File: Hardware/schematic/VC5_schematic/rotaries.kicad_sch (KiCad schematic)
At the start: 9 parts, among them SW1 RotaryEncoder_Switch, SW2 RotaryEncoder_Switch, SW3 RotaryEncoder_Switch, SW4 RotaryEncoder_Switch, SW5 RotaryEncoder_Switch, U7 MCP23017_ML

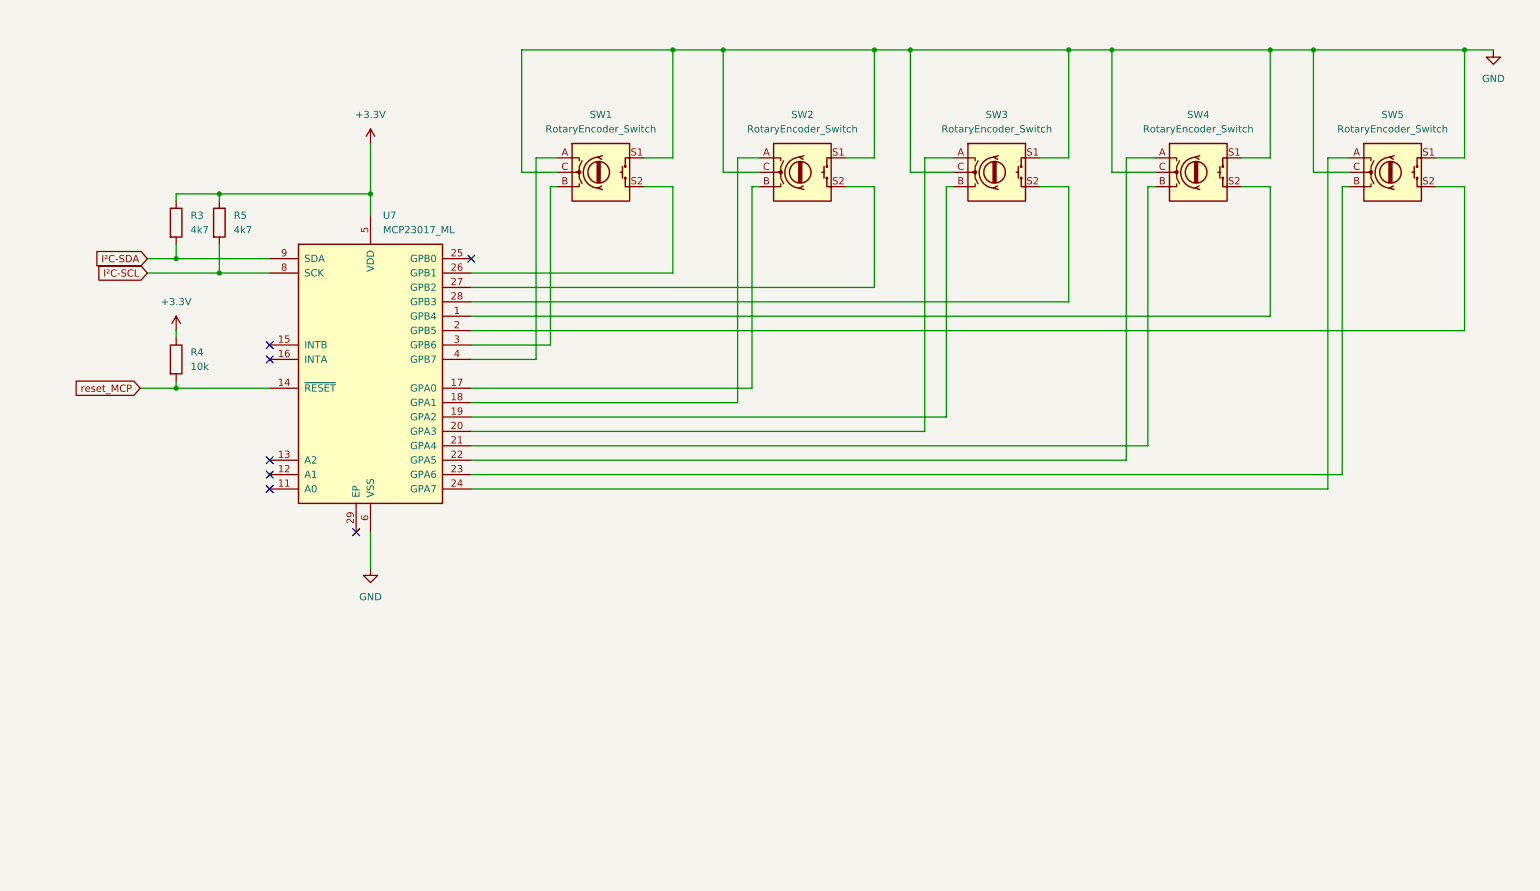
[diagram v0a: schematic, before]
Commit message: minor updates to the schematic
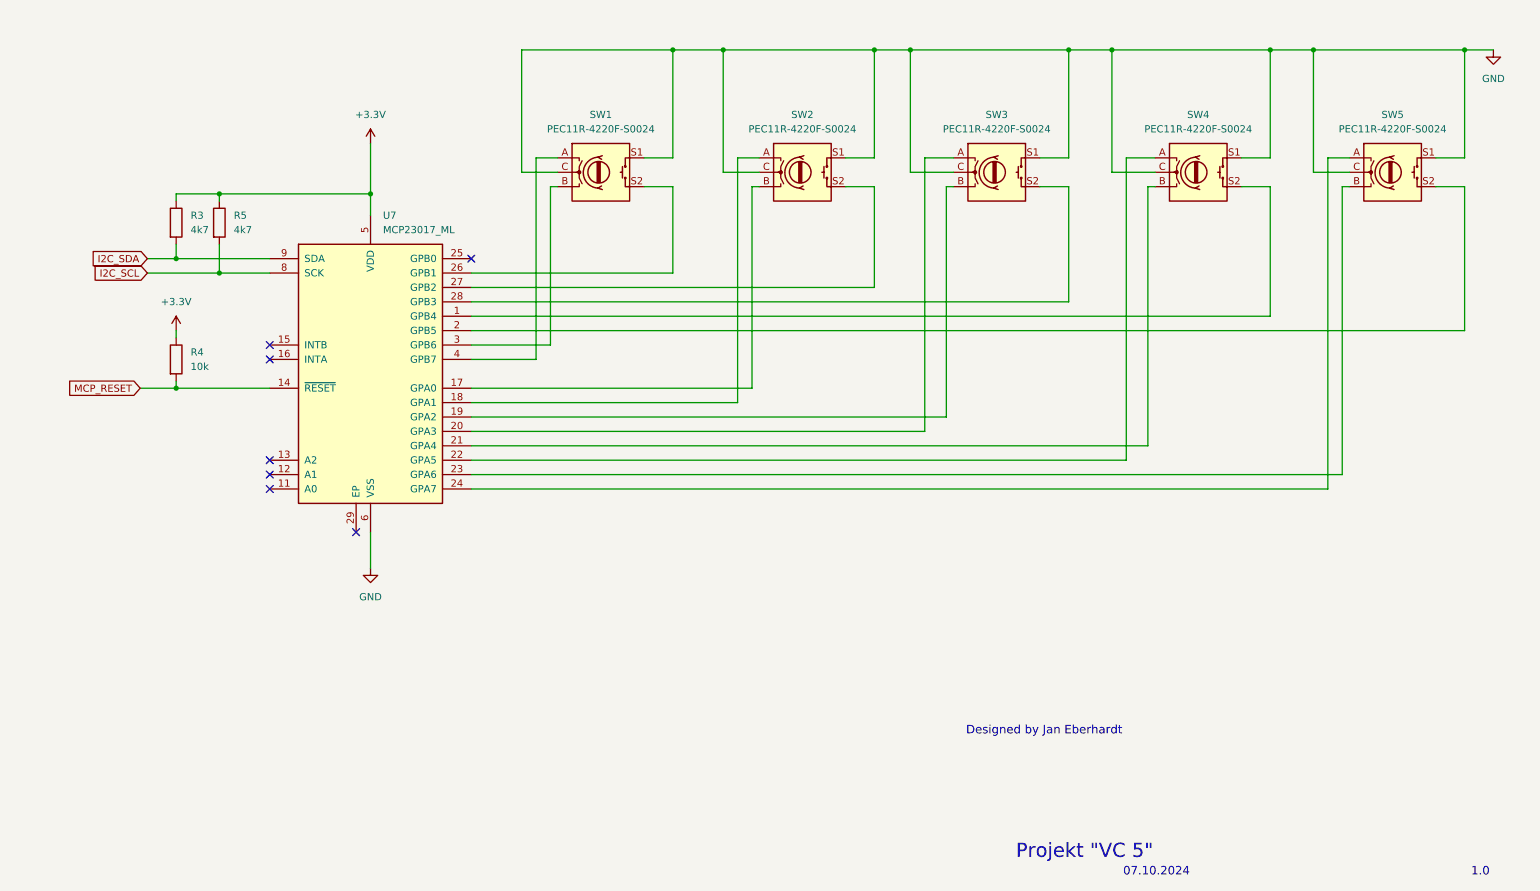
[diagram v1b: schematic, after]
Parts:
- SW1, SW2, SW3, SW4, SW5: value RotaryEncoder_Switch -> PEC11R-4220F-S0024
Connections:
- net I²C-SCL renamed I2C_SCL
- net I²C-SDA renamed I2C_SDA
- net reset_MCP renamed MCP_RESET
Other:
- note added: "07.10.2024"
- note added: "1.0"
- note added: "Designed by Jan Eberhardt"
- note added: "Projekt "VC 5""
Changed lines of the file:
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@@
 		)
 	)
-	(global_label "reset_MCP"
+	(text "Designed by Jan Eberhardt"
+		(exclude_from_sim no)
+		(at 193.802 168.402 0)
+		(effects
+			(font
+				(size 1.5 1.5)
+			)
+		)
+	)
+	(text "07.10.2024"
+		(exclude_from_sim no)
+		(at 213.614 193.294 0)
+		(effects
+			(font
+				(size 1.5 1.5)
+			)
+		)
+	)
+	(text "1.0"
+		(exclude_from_sim no)
+		(at 270.764 193.294 0)
+		(effects
+			(font
+				(size 1.5 1.5)
+			)
+		)
+	)
+	(text "Projekt \"VC 5\""
+		(exclude_from_sim no)
+		(at 200.914 189.738 0)
+		(effects
+			(font
+				(size 2.5 2.5)
+			)
+		)
+	)
+	(global_label "MCP_RESET"
 		(shape input)
 		(at 34.29 107.95 180)
@@
 		)
 		(property "Intersheetrefs" "${INTERSHEET_REFS}"
-			(at 21.6286 107.95 0)
+			(at 21.2549 107.95 0)
 			(effects
 				(font
@@
 		)
 	)
-	(global_label "I²C-SCL"
+	(global_label "I2C_SCL"
 		(shape input)
 		(at 35.56 87.63 180)
@@
 		)
 		(property "Intersheetrefs" "${INTERSHEET_REFS}"
-			(at 24.6524 87.63 0)
+			(at 25.6695 87.63 0)
 			(effects
 				(font
@@
 		)
 	)
-	(global_label "I²C-SDA"
+	(global_label "I2C_SDA"
 		(shape input)
 		(at 35.56 85.09 180)
@@
 		)
 		(property "Intersheetrefs" "${INTERSHEET_REFS}"
-			(at 24.5919 85.09 0)
+			(at 25.609 85.09 0)
 			(effects
 				(font
@@
 			)
 		)
-		(property "Value" "RotaryEncoder_Switch"
+		(property "Value" "PEC11R-4220F-S0024"
 			(at 220.98 62.23 0)
 			(effects
@@
 			)
 		)
-		(property "Value" "RotaryEncoder_Switch"
+		(property "Value" "PEC11R-4220F-S0024"
 			(at 115.57 62.23 0)
 			(effects
@@
 			)
 		)
-		(property "Value" "RotaryEncoder_Switch"
+		(property "Value" "PEC11R-4220F-S0024"
 			(at 185.42 62.23 0)
 			(effects
@@
 			)
 		)
-		(property "Value" "RotaryEncoder_Switch"
+		(property "Value" "PEC11R-4220F-S0024"
 			(at 255.27 62.23 0)
 			(effects
@@
 			)
 		)
-		(property "Value" "RotaryEncoder_Switch"
+		(property "Value" "PEC11R-4220F-S0024"
 			(at 151.13 62.23 0)
 			(effects

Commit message: added missing footprints, changed schematic symbols for the rotaries
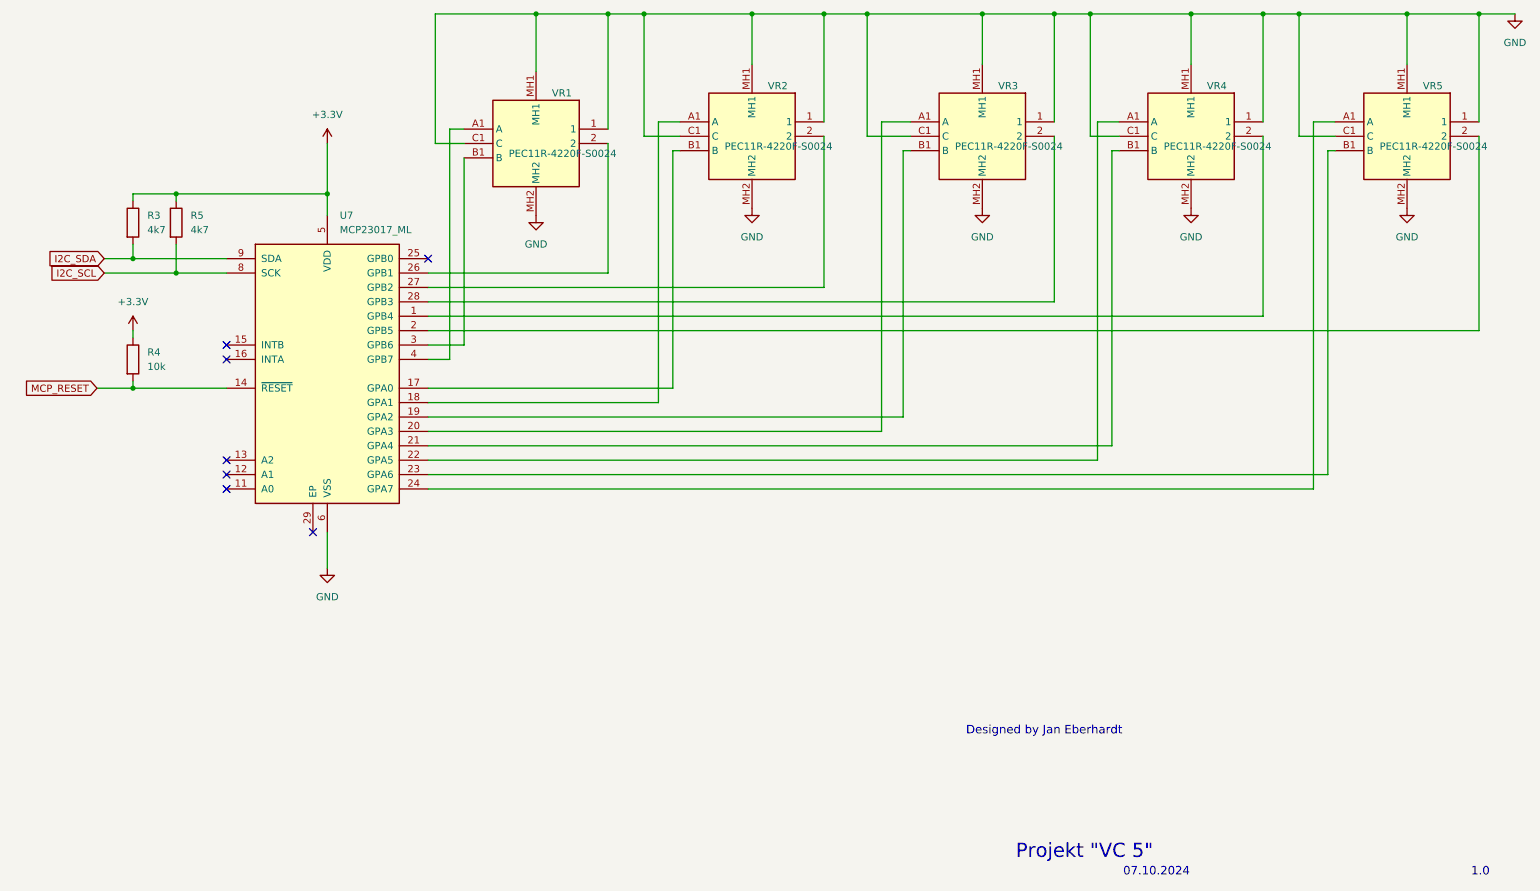
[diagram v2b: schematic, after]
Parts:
- removed SW1, SW2, SW3, SW4, SW5: PEC11R-4220F-S0024, symbol Device:RotaryEncoder_Switch
- added VR1, VR2, VR3, VR4, VR5: PEC11R-4220F-S0024, Bourns_PEC11R:PEC11R4220FS0024, symbol PEC11R-4220F-S0024:PEC11R-4220F-S0024
- R3, R4, R5: footprint (none) -> Resistor_THT:R_Axial_DIN0207_L6.3mm_D2.5mm_P2.54mm_Vertical
- U7: footprint Package_DFN_QFN:QFN-28-1EP_6x6mm_P0.65mm_EP4.25x4.25mm -> MCP23017_IO_expander:MCP23017_IO_expander
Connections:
- net GND: now also VR1.1, VR1.C1 (C), VR1.MH1, VR1.MH2, VR2.1, VR2.C1 (C), VR2.MH1, VR2.MH2, VR3.1, VR3.C1 (C), VR3.MH1, VR3.MH2, VR4.1, VR4.C1 (C), VR4.MH1, VR4.MH2, VR5.1, VR5.C1 (C), VR5.MH1, VR5.MH2
- net at U7.22 (GPA5): now also VR4.A1 (A)
- net at U7.21 (GPA4): now also VR4.B1 (B)
- net at U7.1 (GPB4): now also VR4.2
- net at U7.4 (GPB7): now also VR1.A1 (A)
- net at U7.3 (GPB6): now also VR1.B1 (B)
- net at U7.26 (GPB1): now also VR1.2
- net at U7.20 (GPA3): now also VR3.A1 (A)
- net at U7.19 (GPA2): now also VR3.B1 (B)
- net at U7.28 (GPB3): now also VR3.2
- net at U7.24 (GPA7): now also VR5.A1 (A)
- net at U7.23 (GPA6): now also VR5.B1 (B)
- net at U7.2 (GPB5): now also VR5.2
- net at U7.17 (GPA0): now also VR2.B1 (B)
- net at U7.18 (GPA1): now also VR2.A1 (A)
- net at U7.27 (GPB2): now also VR2.2
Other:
- moved on the sheet: R3, R4, R5

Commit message: first layout
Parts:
- removed U7: MCP23017_ML, MCP23017_IO_expander:MCP23017_IO_expander, symbol Interface_Expansion:MCP23017_ML
- added U7: MCP23017, MCP23017_IO_expander:MCP23017_IO_expander, symbol MCP2307_IO_expander:MCP23017
- R3, R4, R5: footprint Resistor_THT:R_Axial_DIN0207_L6.3mm_D2.5mm_P2.54mm_Vertical -> Resistor_THT:R_Axial_DIN0207_L6.3mm_D2.5mm_P10.16mm_Horizontal
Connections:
- net +3.3V: now also U7.5 (VDD)
- net GND: now also U7.6 (VSS)
- net I2C_SCL: now also U7.8 (SCK)
- net I2C_SDA: now also U7.9 (SDA)
- net MCP_RESET: now also U7.14 (~{RESET})
- net at VR5.2: now also U7.2 (GPB5)
- net at VR5.A1 (A): now also U7.1 (GPB4)
- net at VR5.B1 (B): now also U7.28 (GPB3)
- net at VR1.2: now also U7.19 (GPA2)
- net at VR1.A1 (A): now also U7.18 (GPA1)
- net at VR1.B1 (B): now also U7.17 (GPA0)
- net at VR4.2: now also U7.3 (GPB6)
- net at VR2.B1 (B): now also U7.22 (GPA5)
- net at VR2.A1 (A): now also U7.21 (GPA4)
- net at VR3.B1 (B): now also U7.24 (GPA7)
- net at VR3.A1 (A): now also U7.4 (GPB7)
- net at VR4.B1 (B): now also U7.26 (GPB1)
- net at VR4.A1 (A): now also U7.27 (GPB2)
- net at VR2.2: now also U7.20 (GPA3)
- net at VR3.2: now also U7.23 (GPA6)
- no-connect marks 7 -> 6

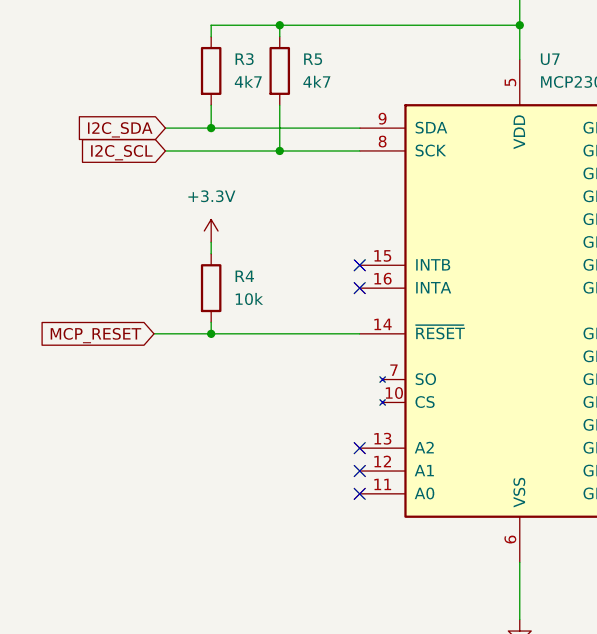
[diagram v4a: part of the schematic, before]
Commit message: added MCP interrupt line
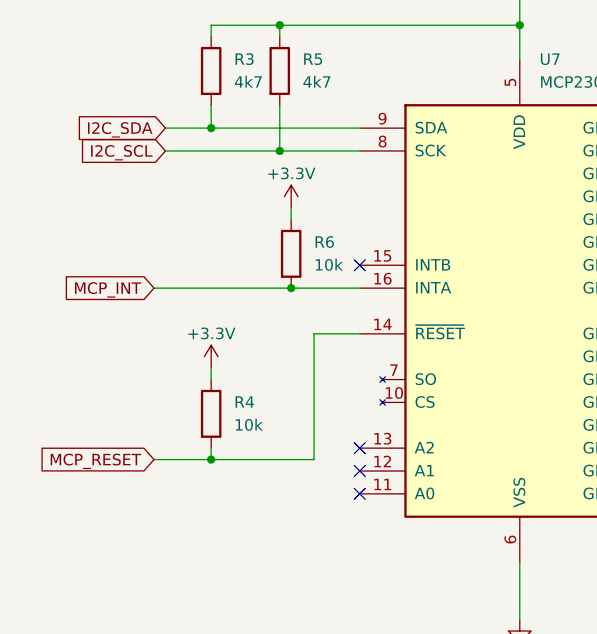
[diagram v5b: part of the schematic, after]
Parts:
- added R6: 10k, Resistor_THT:R_Axial_DIN0207_L6.3mm_D2.5mm_P10.16mm_Horizontal, symbol Device:R
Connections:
- net +3.3V: now also R6.1
- net MCP_INT: now reaches U7.16 (INTA)
- net MCP_INT: now also R6.2
- no-connect marks 6 -> 5
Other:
- moved on the sheet: R4
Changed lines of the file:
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@@
+	)
+	(junction
+		(at 41.91 102.87)
+		(diameter 0)
+		(color 0 0 0 0)
 	)
 	(junction
@@
 	)
 	(junction
-		(at 33.02 107.95)
+		(at 33.02 121.92)
 		(diameter 0)
 		(color 0 0 0 0)
@@
 	)
 	(no_connect
-		(at 49.53 102.87)
-	)
-	(no_connect
 		(at 49.53 123.19)
 	)
@@
 	(wire
 		(pts
-			(xy 26.67 107.95) (xy 33.02 107.95)
+			(xy 26.67 121.92) (xy 33.02 121.92)
+		)
+		(stroke
+			(width 0)
+			(type default)
+		)
+	)
+	(wire
+		(pts
+			(xy 49.53 107.95) (xy 44.45 107.95)
 		)
 		(stroke
@@
 	(wire
 		(pts
-			(xy 33.02 106.68) (xy 33.02 107.95)
+			(xy 41.91 102.87) (xy 49.53 102.87)
+		)
+		(stroke
+			(width 0)
+			(type default)
+		)
+	)
+	(wire
+		(pts
+			(xy 33.02 120.65) (xy 33.02 121.92)
 		)
 		(stroke
@@
 	(wire
 		(pts
-			(xy 33.02 97.79) (xy 33.02 99.06)
+			(xy 33.02 111.76) (xy 33.02 113.03)
 		)
 		(stroke
@@
 	(wire
 		(pts
+			(xy 44.45 107.95) (xy 44.45 121.92)
+		)
+		(stroke
+			(width 0)
+			(type default)
+		)
+	)
+	(wire
+		(pts
 			(xy 129.54 60.96) (xy 125.73 60.96)
 		)
@@
 	(wire
 		(pts
-			(xy 33.02 107.95) (xy 49.53 107.95)
+			(xy 33.02 121.92) (xy 44.45 121.92)
 		)
 		(stroke
@@
 	(wire
 		(pts
+			(xy 41.91 93.98) (xy 41.91 95.25)
+		)
+		(stroke
+			(width 0)
+			(type default)
+		)
+	)
+	(wire
+		(pts
 			(xy 162.56 41.91) (xy 182.88 41.91)
 		)
@@
 		(pts
 			(xy 128.27 66.04) (xy 128.27 120.65)
+		)
+		(stroke
+			(width 0)
+			(type default)
+		)
+	)
+	(wire
+		(pts
+			(xy 26.67 102.87) (xy 41.91 102.87)
 		)
 		(stroke
@@
 	(global_label "MCP_RESET"
 		(shape input)
-		(at 26.67 107.95 180)
+		(at 26.67 121.92 180)
 		(fields_autoplaced yes)
 		(effects
@@
 		)
 		(property "Intersheetrefs" "${INTERSHEET_REFS}"
-			(at 13.6349 107.95 0)
+			(at 13.6349 121.92 0)
 			(effects
 				(font
@@
 		(property "Intersheetrefs" "${INTERSHEET_REFS}"
 			(at 18.0495 87.63 0)
+			(effects
+				(font
+					(size 1.27 1.27)
+				)
+				(justify right)
+				(hide yes)
+			)
+		)
+	)
+	(global_label "MCP_INT"
+		(shape input)
+		(at 26.67 102.87 180)
+		(fields_autoplaced yes)
+		(effects
+			(font
+				(size 1.27 1.27)
+			)
+			(justify right)
+		)
+		(property "Intersheetrefs" "${INTERSHEET_REFS}"
+			(at 16.4771 102.87 0)
 			(effects
 				(font
@@
 	)
 	(symbol
+		(lib_id "Device:R")
+		(at 41.91 99.06 0)
+		(unit 1)
+		(exclude_from_sim no)
+		(in_bom yes)
+		(on_board yes)
+		(dnp no)
+		(fields_autoplaced yes)
+		(property "Reference" "R6"
+			(at 44.45 97.7899 0)
+			(effects
+				(font
+					(size 1.27 1.27)
+				)
+				(justify left)
+			)
+		)
+		(property "Value" "10k"
+			(at 44.45 100.3299 0)
+			(effects
+				(font
+					(size 1.27 1.27)
+				)
+				(justify left)
+			)
+		)
+		(property "Footprint" "Resistor_THT:R_Axial_DIN0207_L6.3mm_D2.5mm_P10.16mm_Horizontal"
+			(at 40.132 99.06 90)
+			(effects
+				(font
+					(size 1.27 1.27)
+				)
+				(hide yes)
+			)
+		)
+		(property "Datasheet" "~"
+			(at 41.91 99.06 0)
+			(effects
+				(font
+					(size 1.27 1.27)
+				)
+				(hide yes)
+			)
+		)
+		(property "Description" "Resistor"
+			(at 41.91 99.06 0)
+			(effects
+				(font
+					(size 1.27 1.27)
+				)
+				(hide yes)
+			)
+		)
+		(pin "1"
+		)
+		(pin "2"
+		)
+		(instances
+			(project "VC5_schematic"
+				(path "/236c86f4-0879-4356-88b2-65461f963bd6/94053ad0-2266-446d-9c80-6f87cfd390a9"
+					(reference "R6")
+					(unit 1)
+				)
+			)
+		)
+	)
+	(symbol
 		(lib_id "power:GND")
 		(at 276.86 41.91 0)
@@
 	(symbol
 		(lib_id "power:+3.3V")
-		(at 33.02 97.79 0)
+		(at 33.02 111.76 0)
 		(unit 1)
 		(exclude_from_sim no)
@@
 		(on_board yes)
 		(dnp no)
-		(fields_autoplaced yes)
 		(property "Reference" "#PWR016"
-			(at 33.02 101.6 0)
+			(at 33.02 115.57 0)
 			(effects
 				(font
@@
 		)
 		(property "Value" "+3.3V"
-			(at 33.02 92.71 0)
+			(at 33.02 107.95 0)
 			(effects
 				(font
@@
 		)
 		(property "Footprint" ""
-			(at 33.02 97.79 0)
+			(at 33.02 111.76 0)
 			(effects
 				(font
@@
 		)
 		(property "Datasheet" ""
-			(at 33.02 97.79 0)
+			(at 33.02 111.76 0)
 			(effects
 				(font
@@
 		)
 		(property "Description" "Power symbol creates a global label with name \"+3.3V\""
-			(at 33.02 97.79 0)
+			(at 33.02 111.76 0)
 			(effects
 				(font
@@
 	(symbol
 		(lib_id "Device:R")
-		(at 33.02 102.87 0)
+		(at 33.02 116.84 0)
 		(unit 1)
 		(exclude_from_sim no)
@@
 		(fields_autoplaced yes)
 		(property "Reference" "R4"
-			(at 35.56 101.5999 0)
+			(at 35.56 115.5699 0)
 			(effects
 				(font
@@
 		)
 		(property "Value" "10k"
-			(at 35.56 104.1399 0)
+			(at 35.56 118.1099 0)
 			(effects
 				(font
@@
 		)
 		(property "Footprint" "Resistor_THT:R_Axial_DIN0207_L6.3mm_D2.5mm_P10.16mm_Horizontal"
-			(at 31.242 102.87 90)
+			(at 31.242 116.84 90)
 			(effects
 				(font
@@
 		)
 		(property "Datasheet" "~"
-			(at 33.02 102.87 0)
+			(at 33.02 116.84 0)
 			(effects
 				(font
@@
 		)
 		(property "Description" "Resistor"
-			(at 33.02 102.87 0)
+			(at 33.02 116.84 0)
 			(effects
 				(font
@@
 					(unit 1)
 				)
+			)
+		)
+	)
+	(symbol
+		(lib_id "power:+3.3V")
+		(at 41.91 93.98 0)
+		(unit 1)
+		(exclude_from_sim no)
+		(in_bom yes)
+		(on_board yes)
+		(dnp no)
+		(property "Reference" "#PWR025"
+			(at 41.91 97.79 0)
+			(effects
+				(font
+					(size 1.27 1.27)
+				)
+				(hide yes)
+			)
+		)
+		(property "Value" "+3.3V"
+			(at 41.91 90.17 0)
+			(effects
+				(font
+					(size 1.27 1.27)
+				)
+			)
+		)
+		(property "Footprint" ""
+			(at 41.91 93.98 0)
+			(effects
+				(font
+					(size 1.27 1.27)
+				)
+				(hide yes)
+			)
+		)
+		(property "Datasheet" ""
+			(at 41.91 93.98 0)
+			(effects
+				(font
+					(size 1.27 1.27)
+				)
+				(hide yes)
+			)
+		)
+		(property "Description" "Power symbol creates a global label with name \"+3.3V\""
+			(at 41.91 93.98 0)
+			(effects
+				(font
+					(size 1.27 1.27)
+				)
+				(hide yes)
+			)
+		)
+		(pin "1"
+		)
+		(instances
+			(project "VC5_schematic"
+				(path "/236c86f4-0879-4356-88b2-65461f963bd6/94053ad0-2266-446d-9c80-6f87cfd390a9"
+					(reference "#PWR025")
+					(unit 1)
+				)
